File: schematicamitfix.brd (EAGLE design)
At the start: 28 x 47 mm, 39 parts, among them J1 FTDI_DEVICE, M1 WIRELESS-NRF24L01, U1 ATMEGA328P_TQFP, U2 GY-521MPU6050, U3 MAX1595EUA33+, Y1 8MHz

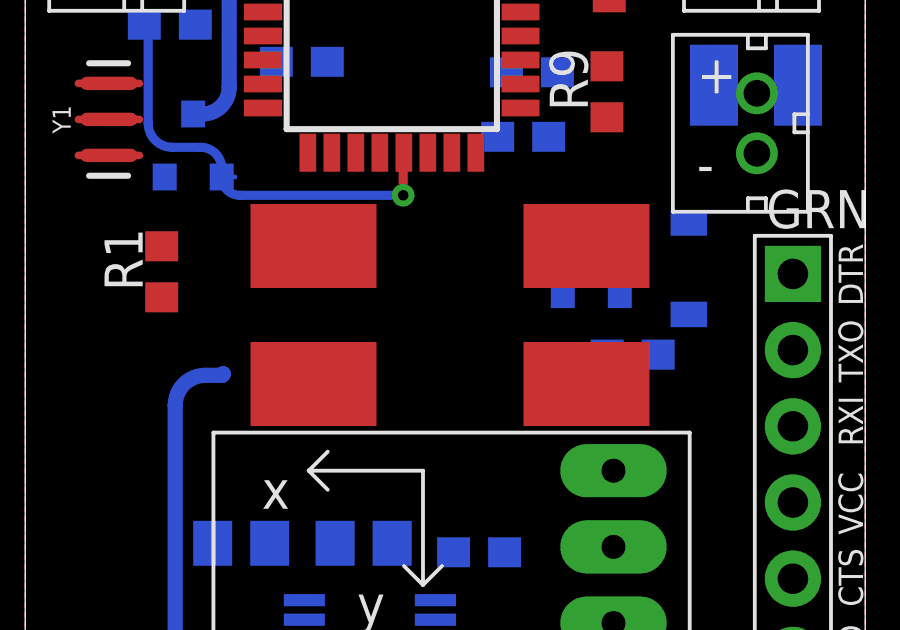
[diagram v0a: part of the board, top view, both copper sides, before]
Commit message: Fixed button library. Somehow I had made the pads 2x too big.
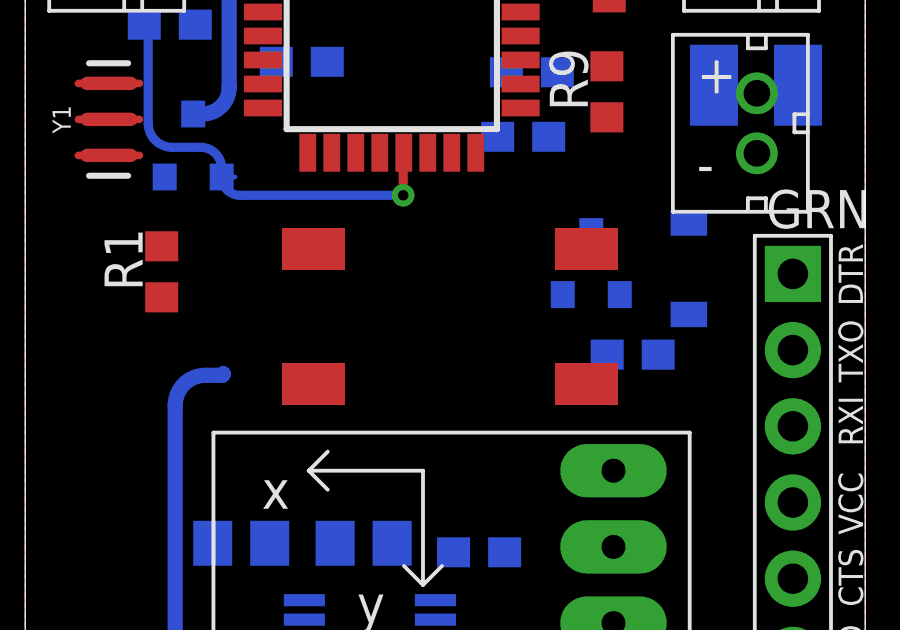
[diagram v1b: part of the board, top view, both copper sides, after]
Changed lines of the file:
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@@
 <wire x1="16.04" y1="36.1" x2="16.5126" y2="38.11" width="0" layer="19" extent="1-16"/>
 <wire x1="4.65" y1="32.61" x2="3.806" y2="34.53" width="0" layer="19" extent="1-16"/>
-<wire x1="5.67" y1="37.69" x2="8.37" y2="36.45" width="0" layer="19" extent="16-16"/>
 <wire x1="15.75" y1="33.95" x2="16.04" y2="36.1" width="0" layer="19" extent="16-16"/>
+<wire x1="5.67" y1="37.69" x2="7.9274" y2="37.31" width="0" layer="19" extent="1-16"/>
 <wire x1="21.1" y1="26.69" x2="18.71" y2="25.71" width="0" layer="19" extent="1-16"/>
 <wire x1="15.75" y1="1.61" x2="14.9" y2="4.46" width="0" layer="19" extent="16-16"/>
@@
 <wire x1="6.55" y1="32.61" x2="7" y2="32.61" width="0.1524" layer="16"/>
 <via x="12.6" y="32" extent="1-16" drill="0.35"/>
-<wire x1="3.97" y1="37.69" x2="7" y2="34.66" width="0" layer="19" extent="1-16"/>
 <wire x1="12.6" y1="32" x2="12.6" y2="33.3974" width="0.3048" layer="1"/>
 <wire x1="12.6" y1="33.3974" x2="12.62" y2="33.4174" width="0.3048" layer="1" curve="-90"/>

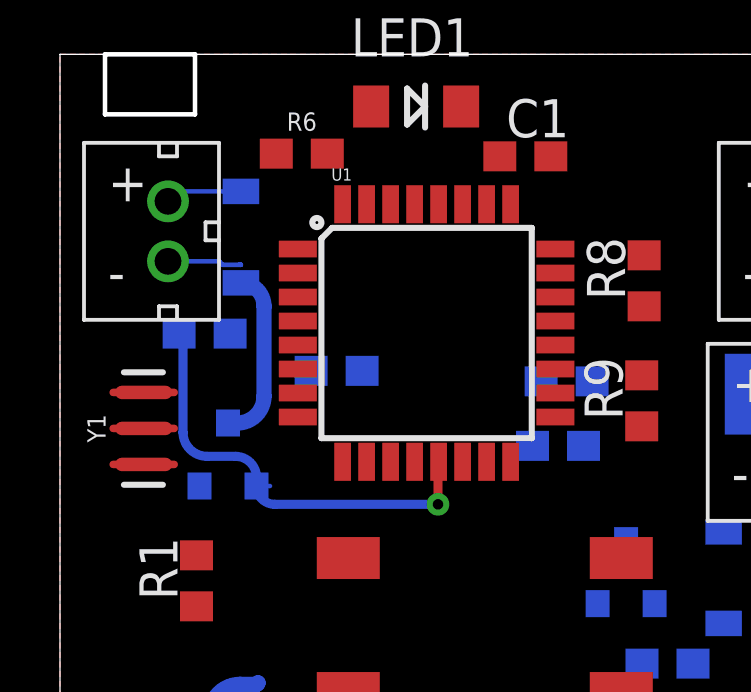
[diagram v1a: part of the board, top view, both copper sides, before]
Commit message: Found the setting for 45 degree routing
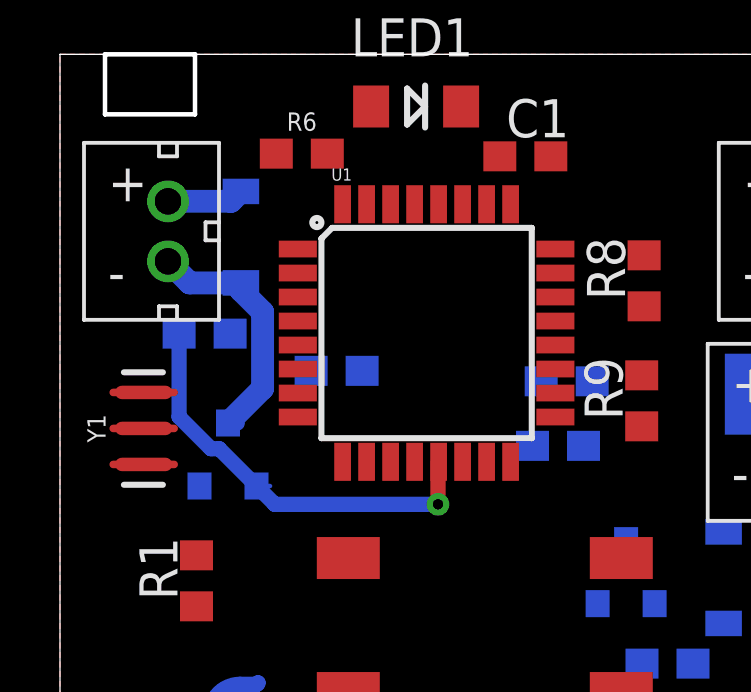
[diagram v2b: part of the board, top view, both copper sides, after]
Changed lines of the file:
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@@
 <wire x1="16.04" y1="36.1" x2="16.5126" y2="38.11" width="0" layer="19" extent="1-16"/>
 <wire x1="4.65" y1="32.61" x2="3.806" y2="34.53" width="0" layer="19" extent="1-16"/>
+<wire x1="5.67" y1="37.69" x2="8.37" y2="36.45" width="0" layer="19" extent="16-16"/>
 <wire x1="15.75" y1="33.95" x2="16.04" y2="36.1" width="0" layer="19" extent="16-16"/>
-<wire x1="5.67" y1="37.69" x2="7.9274" y2="37.31" width="0" layer="19" extent="1-16"/>
 <wire x1="21.1" y1="26.69" x2="18.71" y2="25.71" width="0" layer="19" extent="1-16"/>
 <wire x1="15.75" y1="1.61" x2="14.9" y2="4.46" width="0" layer="19" extent="16-16"/>
@@
 <wire x1="6.55" y1="32.61" x2="7" y2="32.61" width="0.1524" layer="16"/>
 <via x="12.6" y="32" extent="1-16" drill="0.35"/>
-<wire x1="12.6" y1="32" x2="12.6" y2="33.3974" width="0.3048" layer="1"/>
 <wire x1="12.6" y1="33.3974" x2="12.62" y2="33.4174" width="0.3048" layer="1" curve="-90"/>
-<wire x1="12.6" y1="32" x2="7.16" y2="32" width="0.3048" layer="16"/>
-<wire x1="7.16" y1="32" x2="6.55" y2="32.61" width="0.3048" layer="16" curve="-90"/>
-<wire x1="6.55" y1="32.61" x2="6.55" y2="32.9" width="0.3048" layer="16"/>
-<wire x1="6.55" y1="32.9" x2="5.85" y2="33.6" width="0.3048" layer="16" curve="90"/>
-<wire x1="5.85" y1="33.6" x2="4.9" y2="33.6" width="0.3048" layer="16"/>
-<wire x1="4.9" y1="33.6" x2="4.1" y2="34.4" width="0.3048" layer="16" curve="-90"/>
-<wire x1="4.1" y1="34.4" x2="4.1" y2="37.56" width="0.3048" layer="16"/>
+<wire x1="6.55" y1="32.9" x2="6.55" y2="32.61" width="0.3048" layer="16"/>
 <wire x1="4.1" y1="37.56" x2="3.97" y2="37.69" width="0.3048" layer="16" curve="90"/>
+<wire x1="5.0316625" y1="33.8536" x2="5.3064" y2="33.8536" width="0.508" layer="16"/>
+<wire x1="5.3064" y1="33.8536" x2="6.55" y2="32.61" width="0.508" layer="16"/>
+<wire x1="3.97" y1="37.69" x2="3.97" y2="34.9152625" width="0.508" layer="16"/>
+<wire x1="3.97" y1="34.9152625" x2="5.0316625" y2="33.8536" width="0.508" layer="16"/>
+<wire x1="6.55" y1="32.61" x2="7.16" y2="32" width="0.508" layer="16"/>
+<wire x1="7.16" y1="32" x2="12.6" y2="32" width="0.508" layer="16"/>
+<wire x1="12.6" y1="32" x2="12.6" y2="33.3974" width="0.508" layer="1"/>
 </signal>
 <signal name="N$17">
@@
 <contactref element="U$15" pad="-"/>
 <contactref element="U$5" pad="3"/>
-<wire x1="3.6" y1="40.1" x2="5.31" y2="40.1" width="0.1524" layer="16"/>
-<wire x1="5.31" y1="40.1" x2="5.4264" y2="39.9836" width="0.1524" layer="16"/>
-<wire x1="5.4264" y1="39.9836" x2="6.0164" y2="39.9836" width="0.1524" layer="16"/>
-<wire x1="6.03" y1="39.9836" x2="6.0136" y2="40" width="0.1524" layer="16"/>
-<wire x1="6.0136" y1="40" x2="6" y2="40" width="0.1524" layer="16"/>
-<wire x1="6" y1="40" x2="6.0164" y2="39.9836" width="0.1524" layer="16"/>
-<wire x1="6.0164" y1="39.9836" x2="6.03" y2="39.9836" width="0.1524" layer="16"/>
-<wire x1="5.6" y1="34.71" x2="5.91" y2="34.71" width="0.508" layer="16"/>
-<wire x1="5.91" y1="34.71" x2="6.8" y2="35.6" width="0.508" layer="16" curve="90"/>
-<wire x1="6.8" y1="35.6" x2="6.8" y2="38.61" width="0.508" layer="16"/>
-<wire x1="6.8" y1="38.61" x2="6.03" y2="39.38" width="0.508" layer="16" curve="90"/>
-<wire x1="6.03" y1="39.38" x2="6.03" y2="39.9836" width="0" layer="19" extent="16-16"/>
+<wire x1="5.91" y1="34.71" x2="5.6" y2="34.71" width="0.508" layer="16"/>
+<wire x1="6.03" y1="39.38" x2="4.32" y2="39.38" width="0.762" layer="16"/>
+<wire x1="4.32" y1="39.38" x2="3.6" y2="40.1" width="0.762" layer="16"/>
+<wire x1="6.03" y1="39.38" x2="6.03" y2="39.13434375" width="0.762" layer="16"/>
+<wire x1="6.03" y1="39.13434375" x2="6.7534" y2="38.41094375" width="0.762" layer="16"/>
+<wire x1="6.7534" y1="38.41094375" x2="6.7534" y2="35.8634" width="0.762" layer="16"/>
+<wire x1="6.7534" y1="35.8634" x2="5.6" y2="34.71" width="0.762" layer="16"/>
 </signal>
 <signal name="N$7">
@@
 <contactref element="U3" pad="3"/>
 <contactref element="C8" pad="1"/>
-<wire x1="6.03" y1="42.43" x2="3.93" y2="42.43" width="0.1524" layer="16"/>
-<wire x1="3.93" y1="42.43" x2="3.6" y2="42.1" width="0.1524" layer="16"/>
 <wire x1="3.58" y1="13.08" x2="2" y2="11.5" width="0.762" layer="16" curve="90"/>
 <wire x1="2" y1="11.5" x2="2" y2="8" width="0.762" layer="16"/>
 <wire x1="2" y1="8" x2="2.9" y2="7.1" width="0.762" layer="16" curve="90"/>
 <wire x1="2.9" y1="7.1" x2="3.68" y2="7.1" width="0.762" layer="16"/>
+<wire x1="6.03" y1="42.43" x2="5.7" y2="42.1" width="0.762" layer="16"/>
+<wire x1="5.7" y1="42.1" x2="3.6" y2="42.1" width="0.762" layer="16"/>
 <wire x1="19.47" y1="40.3" x2="24.76" y2="42.1" width="0" layer="19" extent="1-1"/>
 <wire x1="22.96" y1="35.67" x2="19.47" y2="40.3" width="0" layer="19" extent="1-16"/>

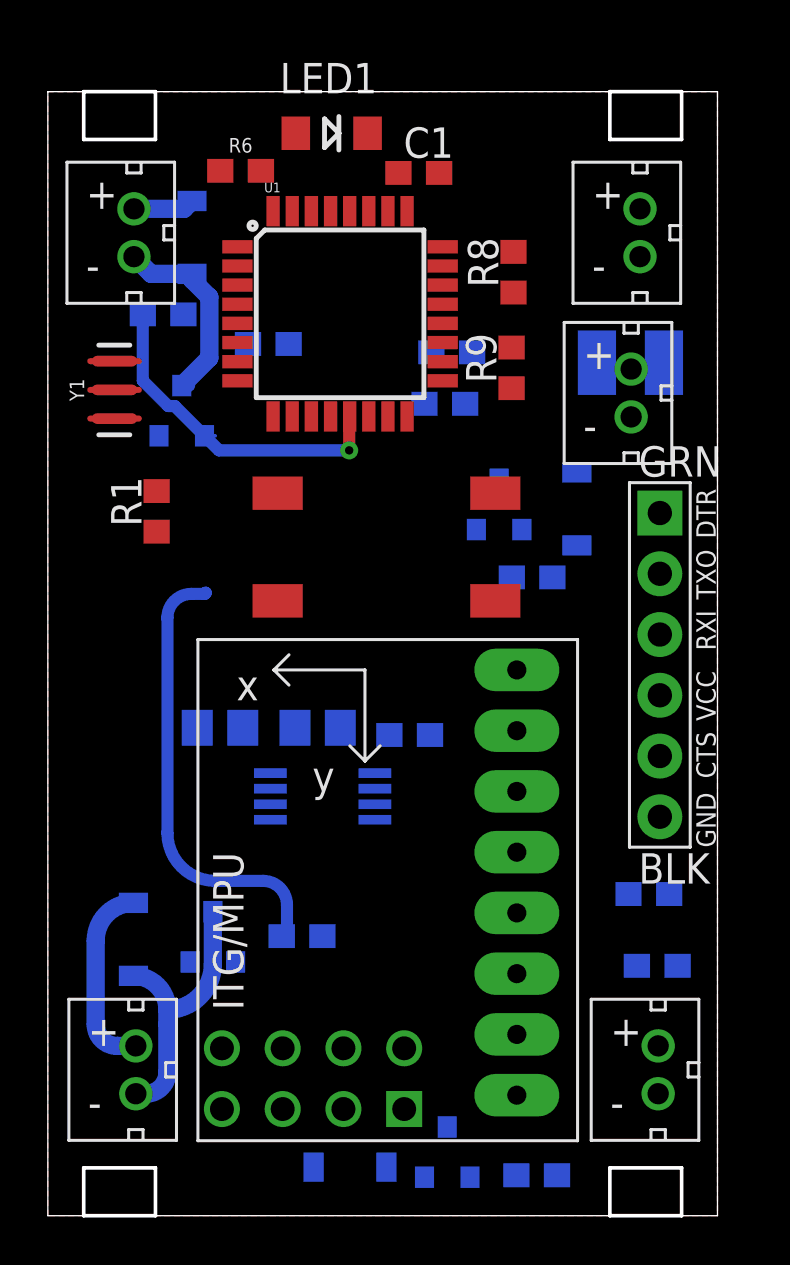
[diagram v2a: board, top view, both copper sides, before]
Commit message: Everything is connected except VCC and GND. But it's really messy and it might even be impossible to connect them successfully without redoing everything.
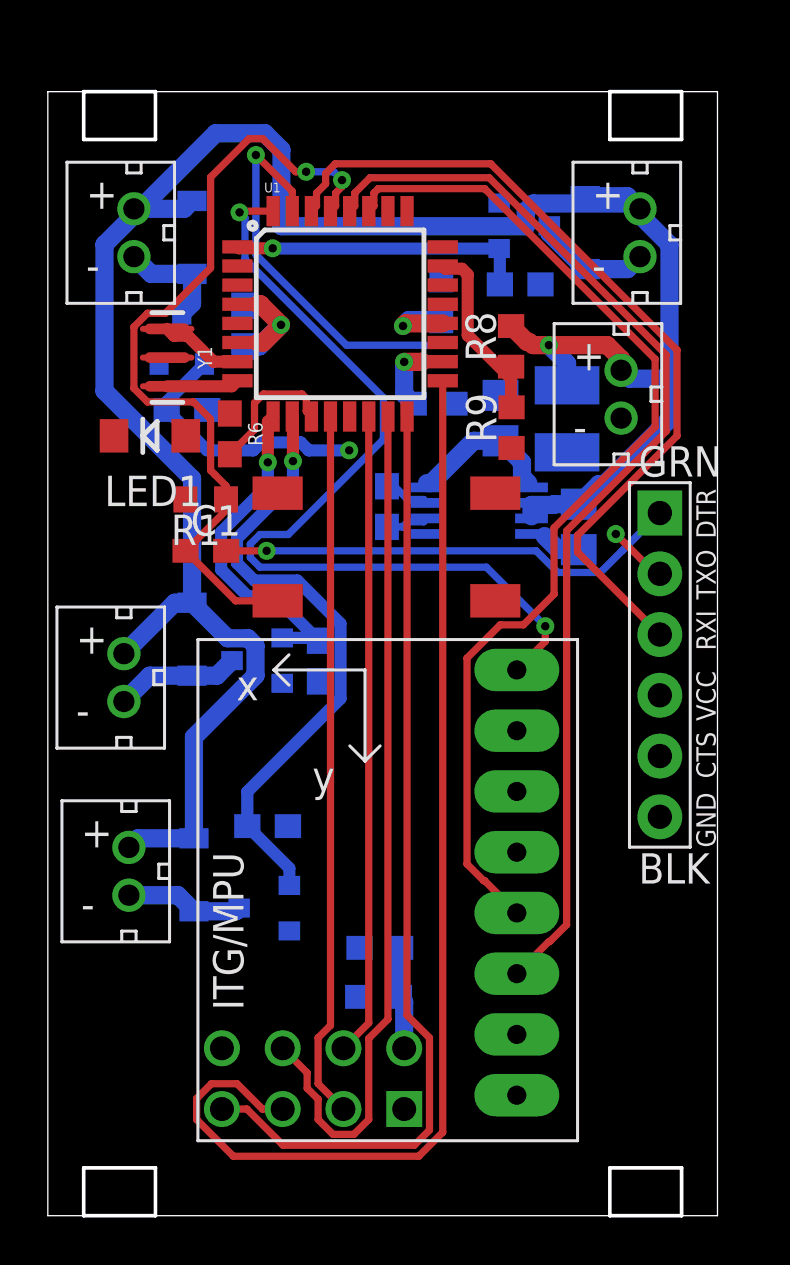
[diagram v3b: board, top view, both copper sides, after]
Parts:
- moved U$3 29.0 mm to (3.39, 14.4)
- moved U$19 28.3 mm to (24.0, 34.4)
- moved R3 18.4 mm to (9.19, 16.3)
- moved C1 18.1 mm to (6.61, 27.8)
- moved C8 17.2 mm to (22.2, 28.8), turned to 270 degrees
- moved U$11 16.4 mm to (3.18, 22.5)
- moved C12 15.0 mm to (18.9, 33.4), turned to 90 degrees
- moved LED1 14.8 mm to (4.27, 32.6), turned to 180 degrees
- moved U$4 13.8 mm to (6.11, 14.2), turned to 0 degrees
- moved U3 13.6 mm to (18.0, 29.5)
- moved U$10 12.8 mm to (6.03, 24.1)
- moved U$9 12.8 mm to (9.10, 12.9), turned to 270 degrees
- moved R2 12.3 mm to (19.8, 38.9)
- moved U$8 11.8 mm to (8.80, 23.2), turned to 270 degrees
- moved U$12 11.7 mm to (19.9, 41.4), turned to 90 degrees
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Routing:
- net VIN: track 10.4 -> 95.9 mm, vias 0 -> 1
- net NRF_SCK: track 0.00 -> 47.9 mm
- net IMU_SCL: track 0.00 -> 45.7 mm
- net IMU_SDA: track 0.00 -> 43.5 mm
- net NRF_MISO: track 0.00 -> 39.8 mm
- net IMU_INT: track 0.00 -> 37.2 mm, vias 0 -> 2
- net NRF_MOSI: track 0.00 -> 36.0 mm
- net FTDI_RX: track 0.00 -> 35.0 mm
- net N$1: track 0.00 -> 33.9 mm, vias 0 -> 2
- net NRF_CE: track 0.00 -> 29.6 mm
- net NRF_CSN: track 0.00 -> 26.9 mm
- net PWM2: track 0.00 -> 25.8 mm, vias 0 -> 1
- net FTDI_DTR: track 0.00 -> 19.5 mm, vias 0 -> 1
- net FTDI_TX: track 0.00 -> 19.0 mm, vias 0 -> 2
- net VCC: track 0.00 -> 17.6 mm, vias 0 -> 2
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- removed copper zone on layer 1, net GND

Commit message: Routed FTDI_TX
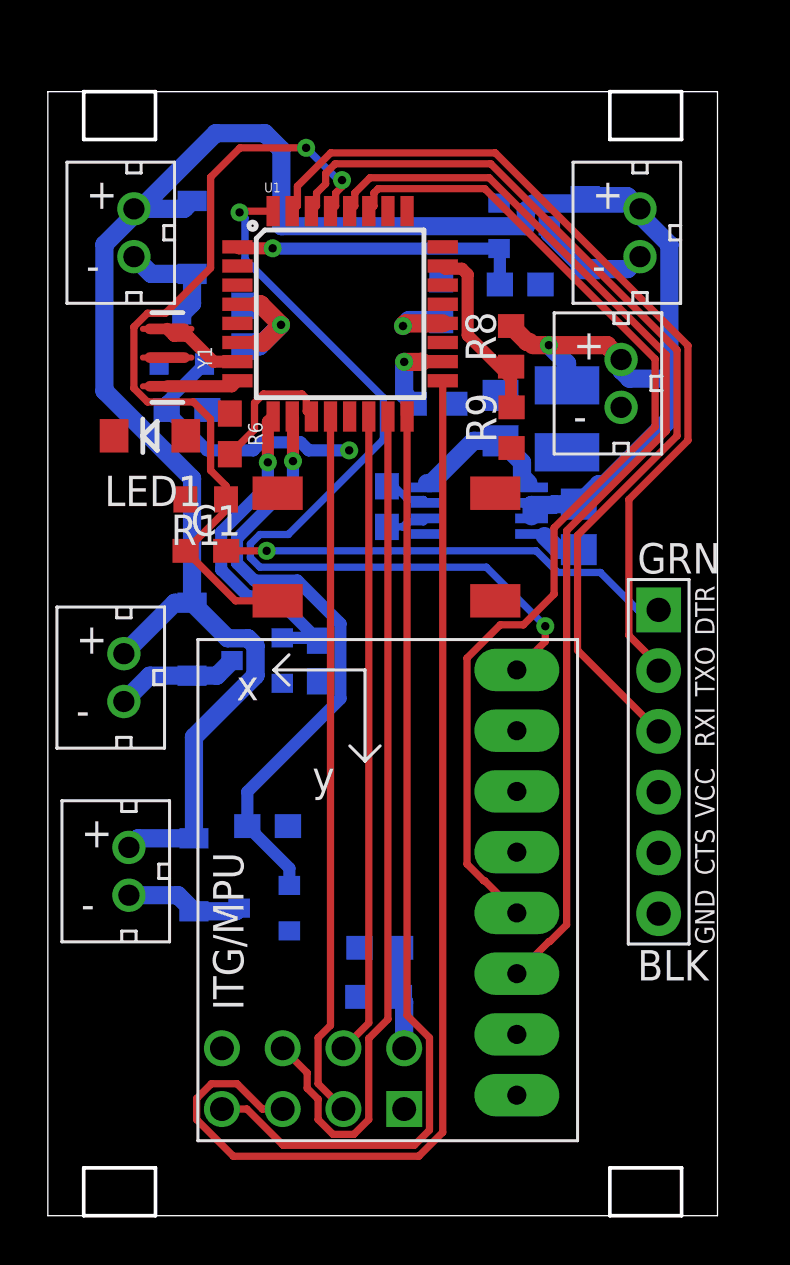
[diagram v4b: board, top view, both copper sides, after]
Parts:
- moved J1 4.05 mm to (25.5, 19.0)
- moved U$19 0.45 mm to (24.0, 34.8)
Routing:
- net FTDI_TX: track 19.0 -> 36.5 mm, vias 2 -> 0
- net FTDI_RX: track 35.0 -> 39.0 mm
